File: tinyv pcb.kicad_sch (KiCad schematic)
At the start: 102 parts, among them J1 JST SH, J2 Pico EZmate, J5 Conn_01x09_Socket, J6 Conn_01x09_Socket, Q1 2N7002, SW1 RST, U1 MCP1700x-330xxTT, U3 STM32F072C8Tx, U4 USBLC6-2SC6

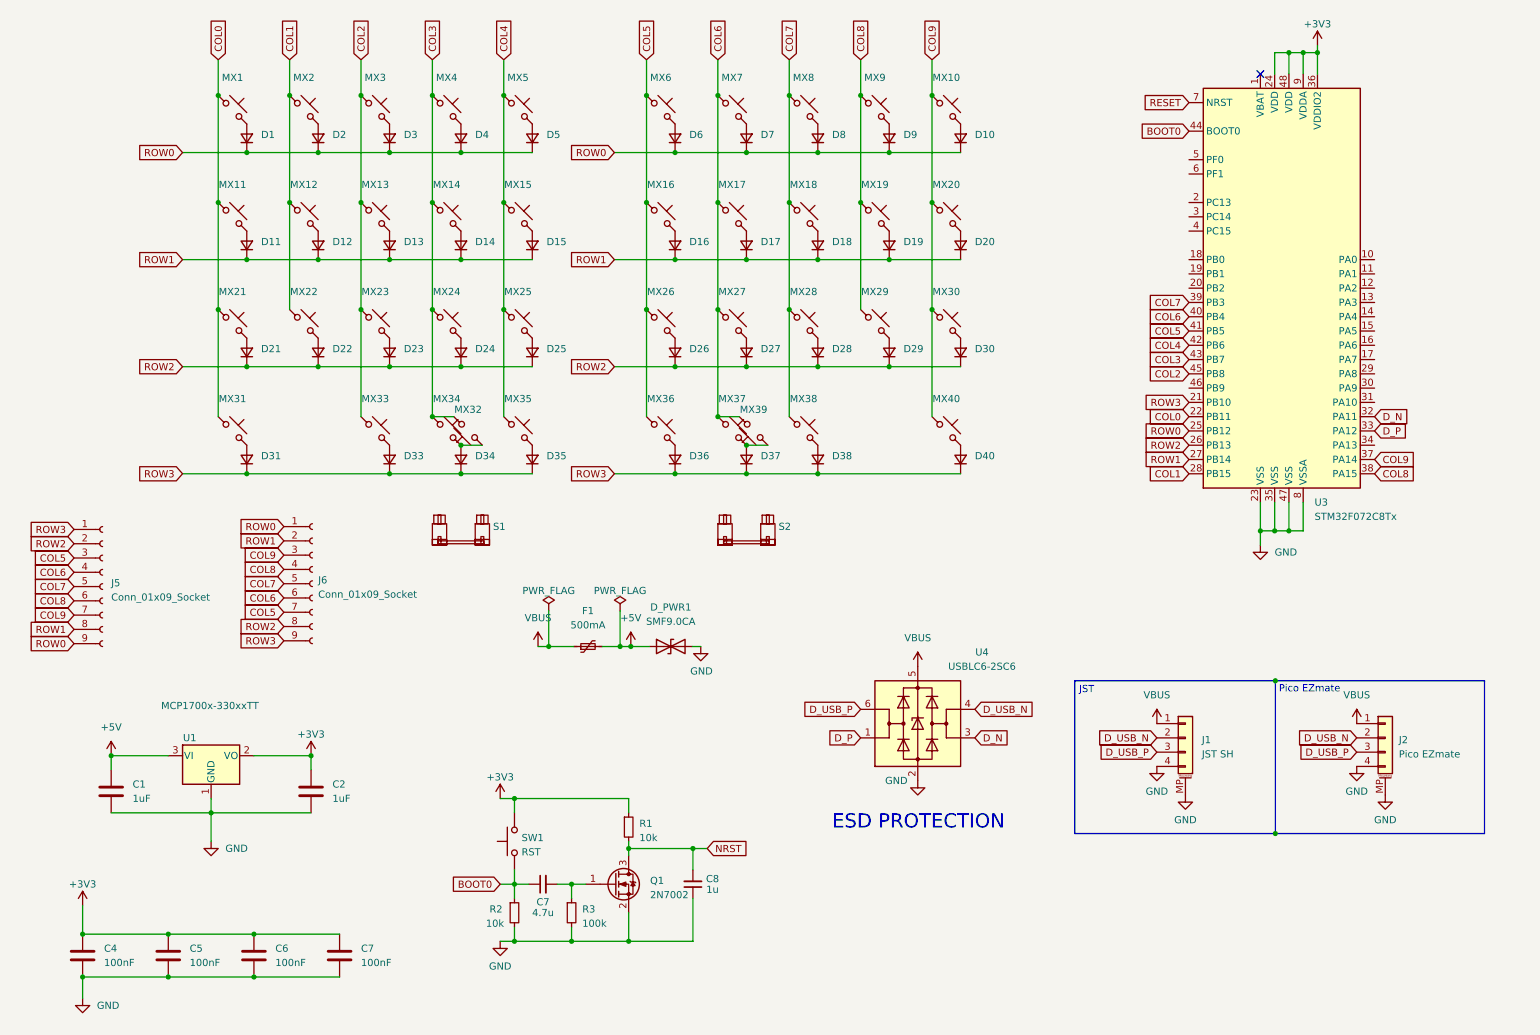
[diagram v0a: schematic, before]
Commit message: routing improvements, error check, cleanup
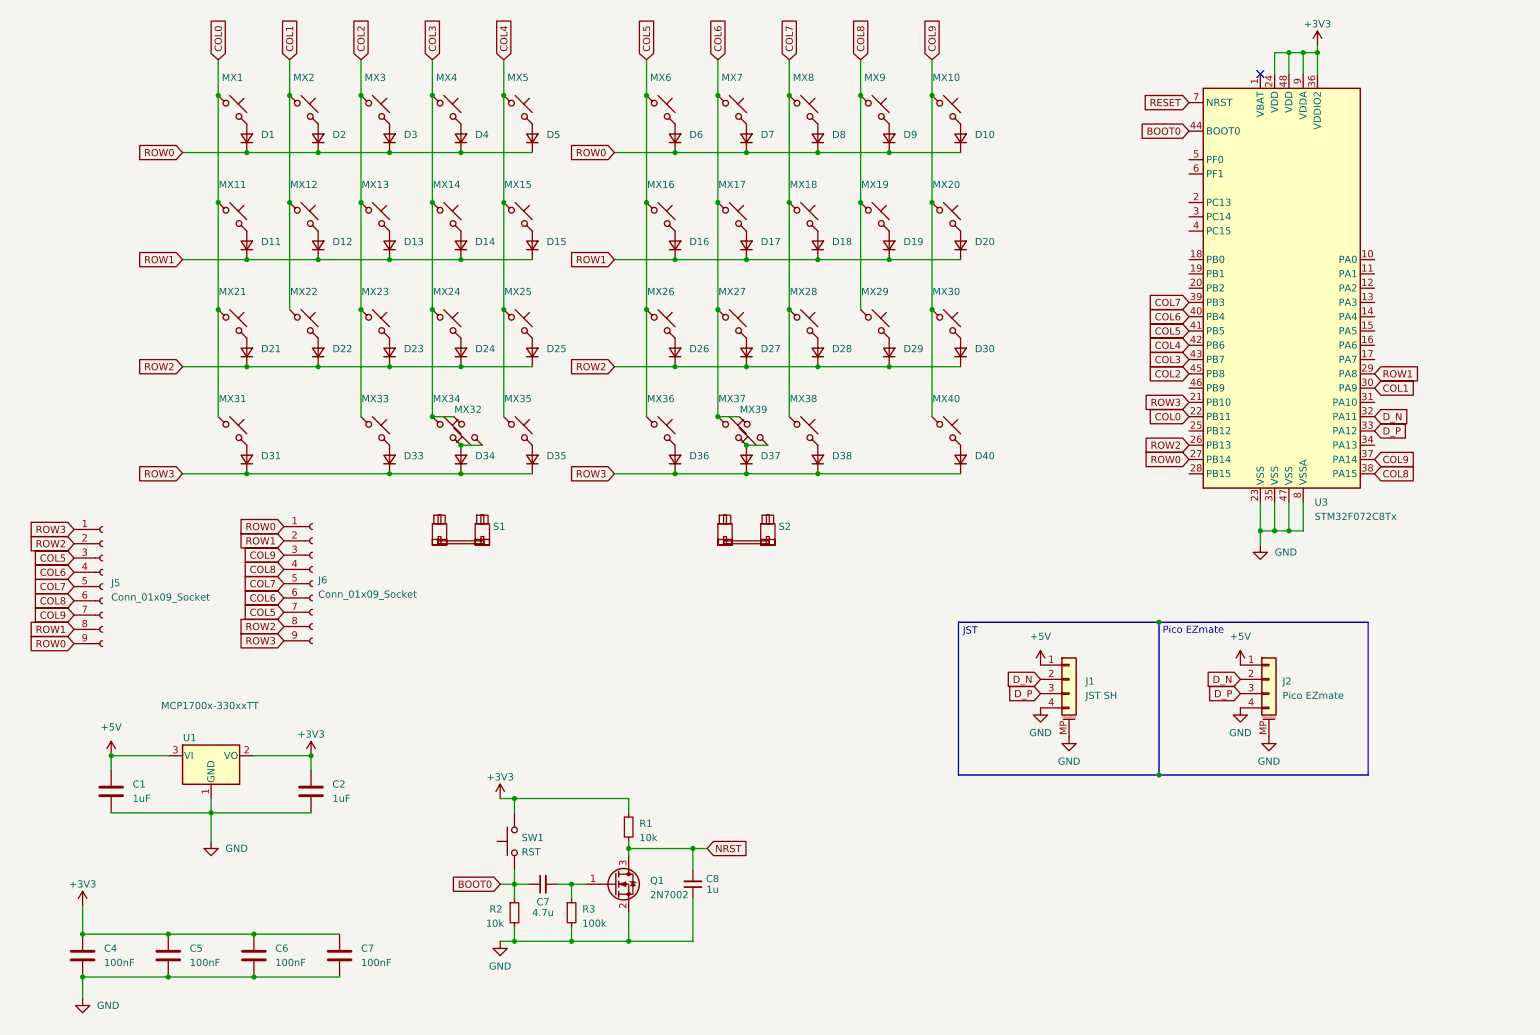
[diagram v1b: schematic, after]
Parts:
- removed D_PWR1: SMF9.0CA, Diode_SMD:D_SOD-123, symbol Device:D_TVS
- removed F1: 500mA, Fuse:Fuse_1206_3216Metric, symbol Device:Polyfuse_Small
- removed U4: USBLC6-2SC6, Package_TO_SOT_SMD:SOT-23-6, symbol Power_Protection:USBLC6-2SC6
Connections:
- net D_USB_N is gone; now on net D_N: J1.2 (Pin_2), J2.2 (Pin_2)
- net D_USB_P is gone; now on net D_P: J1.3 (Pin_3), J2.3 (Pin_3)
- net VBUS is gone; now on net +5V: J1.1 (Pin_1), J2.1 (Pin_1)
- net COL1: now also U3.30 (PA9); no longer U3.28 (PB15)
- net ROW0: now also U3.27 (PB14); no longer U3.25 (PB12)
- net ROW1: now also U3.29 (PA8); no longer U3.27 (PB14)
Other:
- note removed: "ESD PROTECTION"
- moved on the sheet: J1, J2

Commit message: production files & bom, pos missing
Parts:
- added J3: Conn_01x03_Socket, Connector_PinHeader_2.54mm:PinHeader_1x03_P2.54mm_Vertical, symbol Connector:Conn_01x03_Socket
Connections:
- net RESET is gone; now on net NRST: U3.7 (NRST)
- net +5V: now also J3.1 (Pin_1)
- net COL0: now also U3.14 (PA4); no longer U3.22 (PB11)
- net GND: now also J3.3 (Pin_3)
- net ROW3: now also U3.13 (PA3); no longer U3.21 (PB10)
- net underglow: now reaches U3.16 (PA6)
- net underglow: now also J3.2 (Pin_2)
- no-connect marks 1 -> 2
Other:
- note added: "JST connectors for the two pcb halves"
- note added: "MCU caps"
- note added: "MCU power shifter"
- note added: "RGB breakout"
- note added: "reset/boot circuit"
- moved on the sheet: C1, C2, C4, C5, C6, C7, C8, J1, J2, J5, J6, Q1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

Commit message: slight routing change, necessary?
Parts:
- C7: value 4.7u -> 4.7uF
- C8: value 1u -> 1uF
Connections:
- net COL2: now also U3.46 (PB9); no longer U3.45 (PB8)
- net COL3: now also U3.45 (PB8); no longer U3.43 (PB7)
- net COL4: now also U3.43 (PB7); no longer U3.42 (PB6)
- net COL5: now also U3.42 (PB6); no longer U3.41 (PB5)
- net COL6: now also U3.41 (PB5); no longer U3.40 (PB4)
- net COL7: now also U3.40 (PB4); no longer U3.39 (PB3)
- net COL8: now also U3.39 (PB3); no longer U3.38 (PA15)
- no-connect marks 2 -> 7
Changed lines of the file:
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@@
   (junction (at 39.37 174.498) (diameter 0) (color 0 0 0 0)
   )
+  (no_connect (at 223.52 55.88))
+  (no_connect (at 256.54 99.06))
+  (no_connect (at 223.52 50.8))
+  (no_connect (at 256.54 93.98))
+  (no_connect (at 223.52 53.34))
   (no_connect (at 236.22 27.94))
   (no_connect (at 256.54 73.66))
@@
     )
   )
-  (global_label "COL2" (shape input) (at 223.52 81.28 180) (fields_autoplaced)
+  (global_label "COL2" (shape input) (at 223.52 83.82 180) (fields_autoplaced)
     (effects (font (size 1.27 1.27)) (justify right))
-    (property "Intersheetrefs" "${INTERSHEET_REFS}" (at 215.7761 81.28 0)
+    (property "Intersheetrefs" "${INTERSHEET_REFS}" (at 215.7761 83.82 0)
       (effects (font (size 1.27 1.27)) (justify right) hide)
     )
@@
     )
   )
-  (global_label "COL5" (shape input) (at 223.52 73.66 180) (fields_autoplaced)
+  (global_label "COL5" (shape input) (at 223.52 76.2 180) (fields_autoplaced)
     (effects (font (size 1.27 1.27)) (justify right))
-    (property "Intersheetrefs" "${INTERSHEET_REFS}" (at 215.7761 73.66 0)
+    (property "Intersheetrefs" "${INTERSHEET_REFS}" (at 215.7761 76.2 0)
       (effects (font (size 1.27 1.27)) (justify right) hide)
     )
@@
     )
   )
-  (global_label "COL7" (shape input) (at 223.52 68.58 180) (fields_autoplaced)
+  (global_label "COL7" (shape input) (at 223.52 71.12 180) (fields_autoplaced)
     (effects (font (size 1.27 1.27)) (justify right))
-    (property "Intersheetrefs" "${INTERSHEET_REFS}" (at 215.7761 68.58 0)
+    (property "Intersheetrefs" "${INTERSHEET_REFS}" (at 215.7761 71.12 0)
       (effects (font (size 1.27 1.27)) (justify right) hide)
     )
@@
     )
   )
-  (global_label "COL3" (shape input) (at 223.52 78.74 180) (fields_autoplaced)
+  (global_label "COL3" (shape input) (at 223.52 81.28 180) (fields_autoplaced)
     (effects (font (size 1.27 1.27)) (justify right))
-    (property "Intersheetrefs" "${INTERSHEET_REFS}" (at 215.7761 78.74 0)
+    (property "Intersheetrefs" "${INTERSHEET_REFS}" (at 215.7761 81.28 0)
       (effects (font (size 1.27 1.27)) (justify right) hide)
     )
@@
     )
   )
-  (global_label "COL6" (shape input) (at 223.52 71.12 180) (fields_autoplaced)
+  (global_label "COL6" (shape input) (at 223.52 73.66 180) (fields_autoplaced)
     (effects (font (size 1.27 1.27)) (justify right))
-    (property "Intersheetrefs" "${INTERSHEET_REFS}" (at 215.7761 71.12 0)
+    (property "Intersheetrefs" "${INTERSHEET_REFS}" (at 215.7761 73.66 0)
       (effects (font (size 1.27 1.27)) (justify right) hide)
     )
@@
     )
   )
-  (global_label "COL4" (shape input) (at 223.52 76.2 180) (fields_autoplaced)
+  (global_label "COL4" (shape input) (at 223.52 78.74 180) (fields_autoplaced)
     (effects (font (size 1.27 1.27)) (justify right))
-    (property "Intersheetrefs" "${INTERSHEET_REFS}" (at 215.7761 76.2 0)
+    (property "Intersheetrefs" "${INTERSHEET_REFS}" (at 215.7761 78.74 0)
       (effects (font (size 1.27 1.27)) (justify right) hide)
     )
@@
     )
   )
-  (global_label "COL8" (shape input) (at 256.54 99.06 0) (fields_autoplaced)
-    (effects (font (size 1.27 1.27)) (justify left))
-    (property "Intersheetrefs" "${INTERSHEET_REFS}" (at 264.2839 99.06 0)
-      (effects (font (size 1.27 1.27)) (justify left) hide)
+  (global_label "COL8" (shape input) (at 223.52 68.58 180) (fields_autoplaced)
+    (effects (font (size 1.27 1.27)) (justify right))
+    (property "Intersheetrefs" "${INTERSHEET_REFS}" (at 215.7761 68.58 0)
+      (effects (font (size 1.27 1.27)) (justify right) hide)
     )
   )
@@
       (effects (font (size 1.27 1.27)))
     )
-    (property "Value" "1u" (at 64.4525 175.4505 0)
+    (property "Value" "1uF" (at 64.4525 175.4505 0)
       (effects (font (size 1.27 1.27)))
     )
@@
       (effects (font (size 1.27 1.27)))
     )
-    (property "Value" "4.7u" (at 34.29 179.578 90)
+    (property "Value" "4.7uF" (at 34.29 179.578 90)
       (effects (font (size 1.27 1.27)))
     )

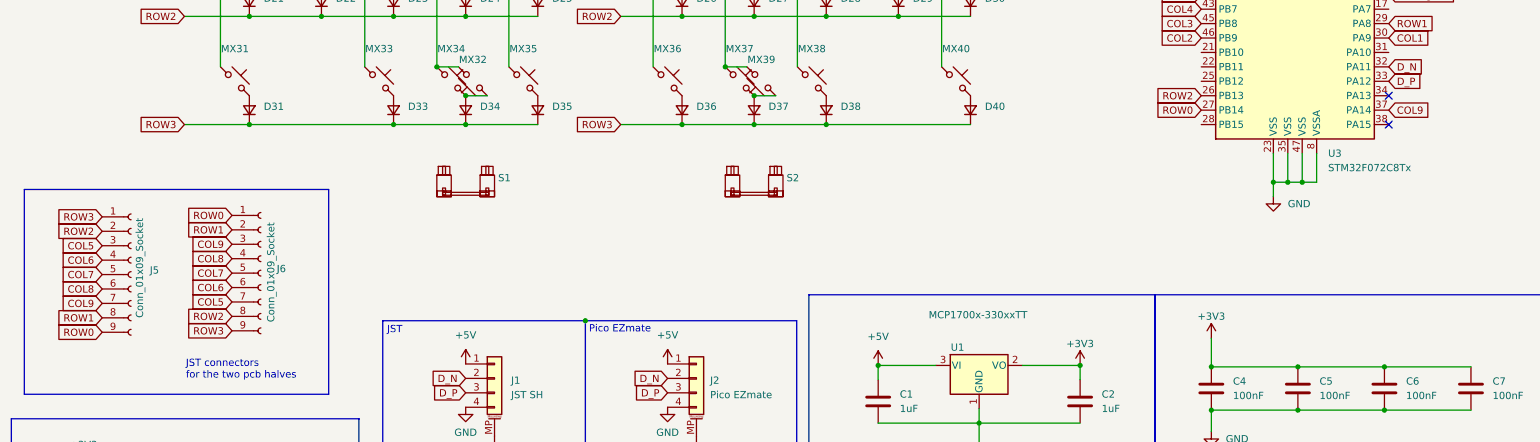
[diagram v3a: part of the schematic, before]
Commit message: production files created
not yet finished
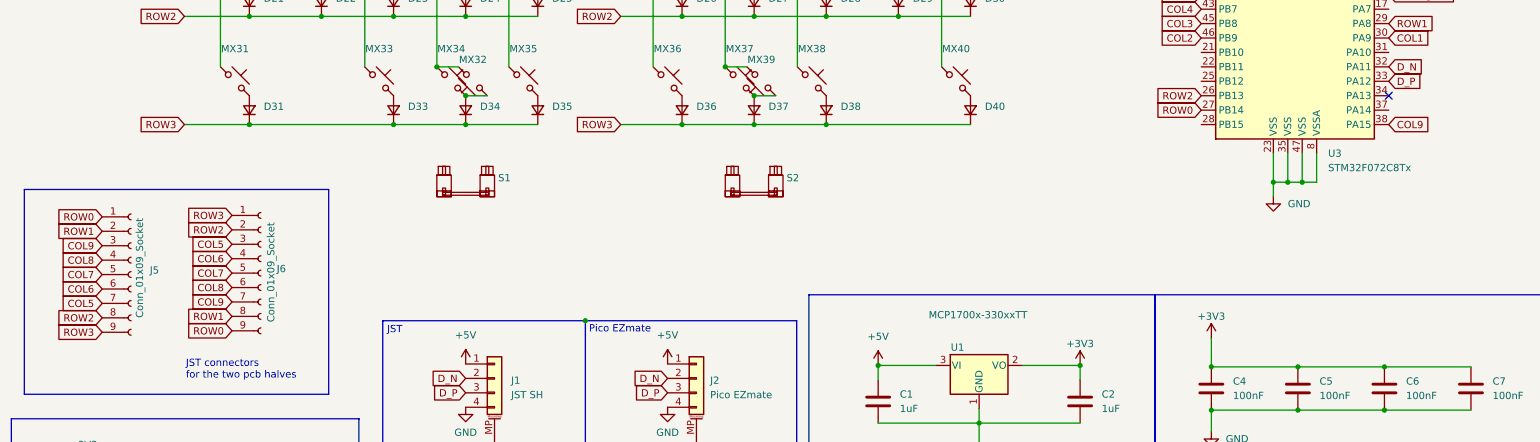
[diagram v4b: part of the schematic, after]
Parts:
- J5, J6: footprint Connector_JST:JST_SH_BM09B-SRSS-TB_1x09-1MP_P1.00mm_Vertical -> Connector_JST:JST_SH_SM09B-SRSS-TB_1x09-1MP_P1.00mm_Horizontal
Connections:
- net COL5: now also J5.7 (Pin_7), J6.3 (Pin_3); no longer J5.3 (Pin_3), J6.7 (Pin_7)
- net COL6: now also J5.6 (Pin_6), J6.4 (Pin_4); no longer J5.4 (Pin_4), J6.6 (Pin_6)
- net COL8: now also J5.4 (Pin_4), J6.6 (Pin_6); no longer J5.6 (Pin_6), J6.4 (Pin_4)
- net COL9: now also J5.3 (Pin_3), J6.7 (Pin_7), U3.38 (PA15); no longer J5.7 (Pin_7), J6.3 (Pin_3), U3.37 (PA14)
- net ROW0: now also J5.1 (Pin_1), J6.9 (Pin_9); no longer J5.9 (Pin_9), J6.1 (Pin_1)
- net ROW1: now also J5.2 (Pin_2), J6.8 (Pin_8); no longer J5.8 (Pin_8), J6.2 (Pin_2)
- net ROW2: now also J5.8 (Pin_8), J6.2 (Pin_2); no longer J5.2 (Pin_2), J6.8 (Pin_8)
- net ROW3: now also J5.9 (Pin_9), J6.1 (Pin_1); no longer J5.1 (Pin_1), J6.9 (Pin_9)
- no-connect marks 7 -> 6
